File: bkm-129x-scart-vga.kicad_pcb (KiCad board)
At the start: 2 copper layers, 105 x 160 mm, 69 parts, among them J1 DB15_Female_HighDensity_Mount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, J2 SCART-F, J3 SJ1-353XNG, J4 UART, J5 Conn_02x32_Row_Letter_Last, J6 ICSP, Q1 DTC144EKA, Q2 MMBT3904, SW1 PBH4UEENAGX, SW2 PBH4UEENAGX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

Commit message: Add github link to PCB silkscreen.
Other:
- board text added: "(2020) Martin Hejnfelt (martin@hejnfelt.com) www.immerhax.com Mod github.com/proboterror/bkm-129x-scart-vga"
- board text removed: "(2020) Martin Hejnfelt (martin@hejnfelt.com) www.immerhax.com"
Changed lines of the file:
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@@
 		(layer "Edge.Cuts")
 	)
-	(gr_text "(2020) Martin Hejnfelt (martin@hejnfelt.com)\nwww.immerhax.com"
+	(gr_text "(2020) Martin Hejnfelt (martin@hejnfelt.com)\nwww.immerhax.com\n\nMod github.com/proboterror/bkm-129x-scart-vga"
 		(at 115.7478 50.3936 0)
 		(layer "B.SilkS")

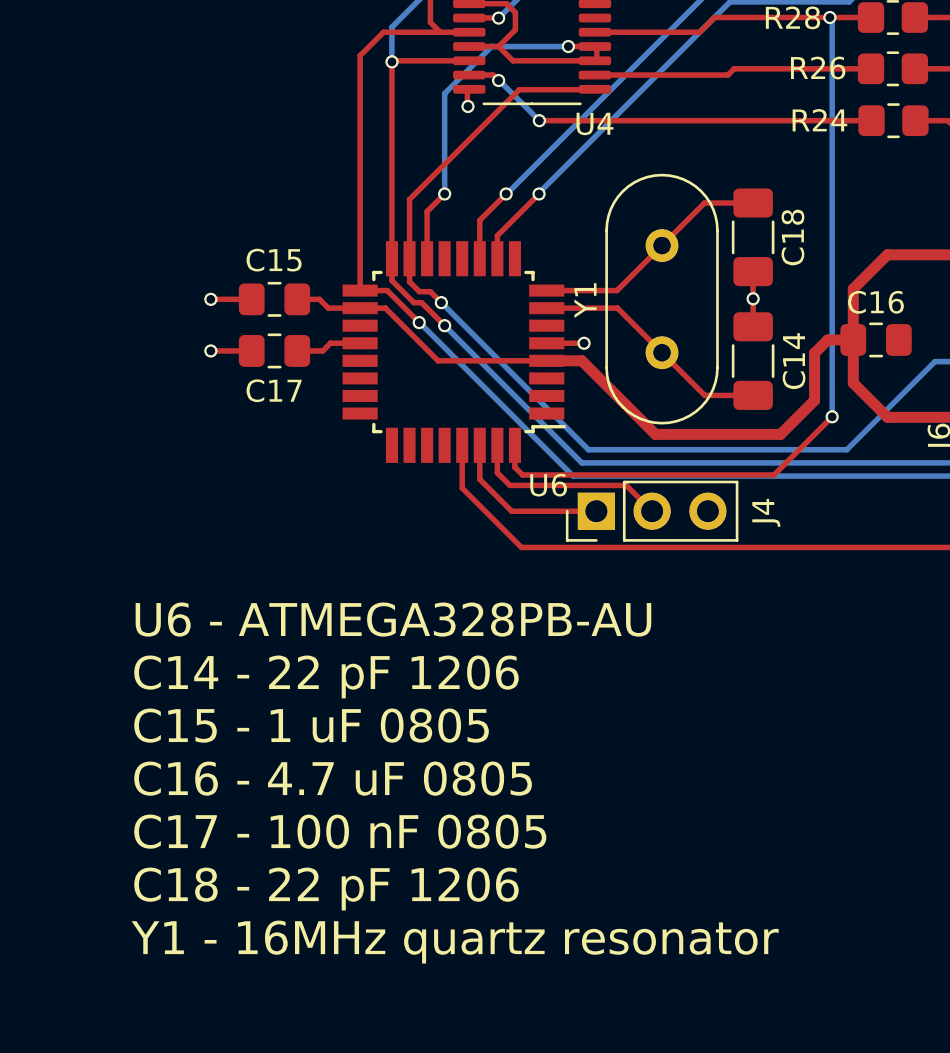
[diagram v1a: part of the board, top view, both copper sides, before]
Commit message: Change C14, C18 footprints from 1206 to 0805.
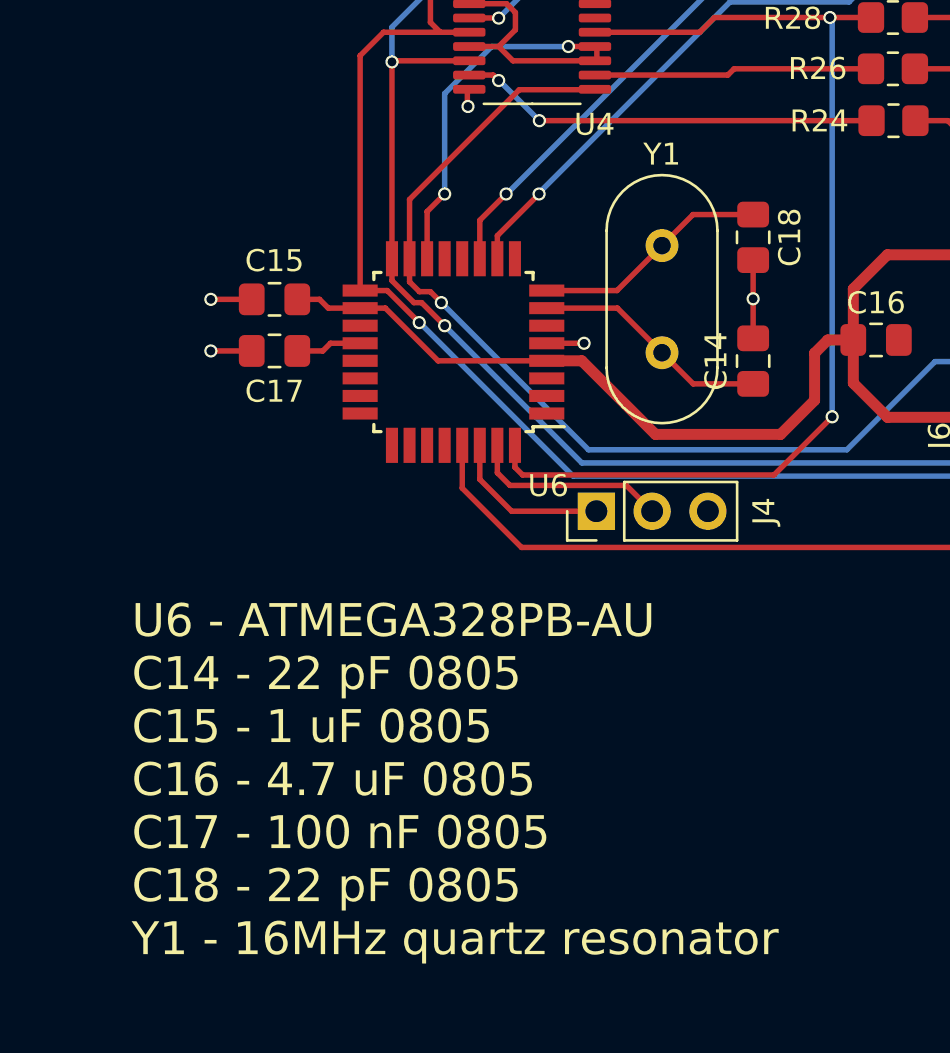
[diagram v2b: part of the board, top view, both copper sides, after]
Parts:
- C14, C18: footprint Capacitor_SMD:C_1206_3216Metric_Pad1.33x1.80mm_HandSolder -> Capacitor_SMD:C_0805_2012Metric_Pad1.18x1.45mm_HandSolder
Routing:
- net GNDA: track 20.5 -> 21.6 mm
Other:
- board text added: "U6 - ATMEGA328PB-AU C14 - 22 pF 0805 C15 - 1 uF 0805 C16 - 4.7 uF 0805 C17 - 100 nF 0805 C18 - 22 pF 0805 Y1 - 16MHz quartz resonator"
- board text removed: "U6 - ATMEGA328PB-AU C14 - 22 pF 1206 C15 - 1 uF 0805 C16 - 4.7 uF 0805 C17 - 100 nF 0805 C18 - 22 pF 1206 Y1 - 16MHz quartz resonator"
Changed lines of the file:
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@@
 		(tags "THT crystalHC-49/U")
 		(property "Reference" "Y1"
-			(at 2.44 3.45 90)
+			(at -4.15 0 180)
 			(layer "F.SilkS")
 			(effects
@@
 		)
 	)
-	(footprint "Capacitor_SMD:C_1206_3216Metric_Pad1.33x1.80mm_HandSolder"
+	(footprint "Capacitor_SMD:C_0805_2012Metric_Pad1.18x1.45mm_HandSolder"
 		(layer "F.Cu")
 		(at 110.6 134.675 -90)
-		(descr "Capacitor SMD 1206 (3216 Metric), square (rectangular) end terminal, IPC_7351 nominal with elongated pad for handsoldering. (Body size source: IPC-SM-782 page 76, https://www.pcb-3d.com/wordpress/wp-content/uploads/ipc-sm-782a_amendment_1_and_2.pdf), generated with kicad-footprint-generator")
+		(descr "Capacitor SMD 0805 (2012 Metric), square (rectangular) end terminal, IPC_7351 nominal with elongated pad for handsoldering. (Body size source: IPC-SM-782 page 76, https://www.pcb-3d.com/wordpress/wp-content/uploads/ipc-sm-782a_amendment_1_and_2.pdf, https://docs.google.com/spreadsheets/d/1BsfQQcO9C6DZCsRaXUlFlo91Tg2WpOkGARC1WS5S8t0/edit?usp=sharing), generated with kicad-footprint-generator")
 		(tags "capacitor handsolder")
 		(property "Reference" "C18"
-			(at 0 -1.85 90)
+			(at 0 -1.68 -90)
 			(layer "F.SilkS")
 			(effects
@@
 		)
 		(property "Value" "22pF"
-			(at 0.15 1.85 90)
+			(at 0 1.68 -90)
 			(layer "F.Fab")
 			(effects
@@
 			)
 		)
-		(property ki_fp_filters "C_*")
-		(sheetname "MCU")
-		(sheetfile "atmega328p.kicad_sch")
 		(attr smd)
 		(fp_line
-			(start -0.711252 0.91)
-			(end 0.711252 0.91)
+			(start -0.261252 0.735)
+			(end 0.261252 0.735)
 			(stroke
 				(width 0.12)
@@
 		)
 		(fp_line
-			(start -0.711252 -0.91)
-			(end 0.711252 -0.91)
+			(start -0.261252 -0.735)
+			(end 0.261252 -0.735)
 			(stroke
 				(width 0.12)
@@
 		)
 		(fp_line
-			(start -2.48 1.15)
-			(end -2.48 -1.15)
+			(start -1.88 0.98)
+			(end -1.88 -0.98)
 			(stroke
 				(width 0.05)
@@
 		)
 		(fp_line
-			(start 2.48 1.15)
-			(end -2.48 1.15)
+			(start 1.88 0.98)
+			(end -1.88 0.98)
 			(stroke
 				(width 0.05)
@@
 		)
 		(fp_line
-			(start -2.48 -1.15)
-			(end 2.48 -1.15)
+			(start -1.88 -0.98)
+			(end 1.88 -0.98)
 			(stroke
 				(width 0.05)
@@
 		)
 		(fp_line
-			(start 2.48 -1.15)
-			(end 2.48 1.15)
+			(start 1.88 -0.98)
+			(end 1.88 0.98)
 			(stroke
 				(width 0.05)
@@
 		)
 		(fp_line
-			(start -1.6 0.8)
-			(end -1.6 -0.8)
+			(start -1 0.625)
+			(end -1 -0.625)
 			(stroke
 				(width 0.1)
@@
 		)
 		(fp_line
-			(start 1.6 0.8)
-			(end -1.6 0.8)
+			(start 1 0.625)
+			(end -1 0.625)
 			(stroke
 				(width 0.1)
@@
 		)
 		(fp_line
-			(start -1.6 -0.8)
-			(end 1.6 -0.8)
+			(start -1 -0.625)
+			(end 1 -0.625)
 			(stroke
 				(width 0.1)
@@
 		)
 		(fp_line
-			(start 1.6 -0.8)
-			(end 1.6 0.8)
+			(start 1 -0.625)
+			(end 1 0.625)
 			(stroke
 				(width 0.1)
@@
 		)
 		(fp_text user "${REFERENCE}"
-			(at 0 0 90)
+			(at 0 0 -90)
 			(layer "F.Fab")
 			(effects
 				(font
-					(size 0.8 0.8)
-					(thickness 0.12)
+					(size 0.5 0.5)
+					(thickness 0.08)
 				)
 			)
 		)
 		(pad "1" smd roundrect
-			(at -1.5625 0 270)
-			(size 1.325 1.8)
+			(at -1.0375 0 270)
+			(size 1.175 1.45)
 			(layers "F.Cu" "F.Paste" "F.Mask")
-			(roundrect_rratio 0.188679)
+			(roundrect_rratio 0.212766)
 			(net 11 "Net-(U6-(XTAL2{slash}TOSC2)PB7)")
 			(pintype "passive")
 		)
 		(pad "2" smd roundrect
-			(at 1.5625 0 270)
-			(size 1.325 1.8)
+			(at 1.0375 0 270)
+			(size 1.175 1.45)
 			(layers "F.Cu" "F.Paste" "F.Mask")
-			(roundrect_rratio 0.188679)
+			(roundrect_rratio 0.212766)
 			(net 6 "GNDA")
 			(pintype "passive")
 		)
-		(model "${KICAD8_3DMODEL_DIR}/Capacitor_SMD.3dshapes/C_1206_3216Metric.wrl"
+		(model "${KICAD8_3DMODEL_DIR}/Capacitor_SMD.3dshapes/C_0805_2012Metric.wrl"
 			(offset
 				(xyz 0 0 0)
@@
 		)
 	)
-	(footprint "Capacitor_SMD:C_1206_3216Metric_Pad1.33x1.80mm_HandSolder"
+	(footprint "Capacitor_SMD:C_0805_2012Metric_Pad1.18x1.45mm_HandSolder"
 		(layer "F.Cu")
 		(at 110.6 140.3125 90)
-		(descr "Capacitor SMD 1206 (3216 Metric), square (rectangular) end terminal, IPC_7351 nominal with elongated pad for handsoldering. (Body size source: IPC-SM-782 page 76, https://www.pcb-3d.com/wordpress/wp-content/uploads/ipc-sm-782a_amendment_1_and_2.pdf), generated with kicad-footprint-generator")
+		(descr "Capacitor SMD 0805 (2012 Metric), square (rectangular) end terminal, IPC_7351 nominal with elongated pad for handsoldering. (Body size source: IPC-SM-782 page 76, https://www.pcb-3d.com/wordpress/wp-content/uploads/ipc-sm-782a_amendment_1_and_2.pdf, https://docs.google.com/spreadsheets/d/1BsfQQcO9C6DZCsRaXUlFlo91Tg2WpOkGARC1WS5S8t0/edit?usp=sharing), generated with kicad-footprint-generator")
 		(tags "capacitor handsolder")
 		(property "Reference" "C14"
-			(at 0 1.9 -90)
+			(at 0 -1.68 90)
 			(layer "F.SilkS")
 			(effects
@@
 		)
 		(property "Value" "22pF"
-			(at 0 -1.85 -90)
+			(at 0 1.68 90)
 			(layer "F.Fab")
 			(effects
@@
 			)
 		)
-		(property ki_fp_filters "C_*")
-		(sheetname "MCU")
-		(sheetfile "atmega328p.kicad_sch")
 		(attr smd)
 		(fp_line
-			(start -0.711252 -0.91)
-			(end 0.711252 -0.91)
+			(start -0.261252 -0.735)
+			(end 0.261252 -0.735)
 			(stroke
 				(width 0.12)
@@
 		)
 		(fp_line
-			(start -0.711252 0.91)
-			(end 0.711252 0.91)
+			(start -0.261252 0.735)
+			(end 0.261252 0.735)
 			(stroke
 				(width 0.12)
@@
 		)
 		(fp_line
-			(start 2.48 -1.15)
-			(end 2.48 1.15)
+			(start 1.88 -0.98)
+			(end 1.88 0.98)
 			(stroke
 				(width 0.05)
@@
 		)
 		(fp_line
-			(start -2.48 -1.15)
-			(end 2.48 -1.15)
+			(start -1.88 -0.98)
+			(end 1.88 -0.98)
 			(stroke
 				(width 0.05)
@@
 		)
 		(fp_line
-			(start 2.48 1.15)
-			(end -2.48 1.15)
+			(start 1.88 0.98)
+			(end -1.88 0.98)
 			(stroke
 				(width 0.05)
@@
 		)
 		(fp_line
-			(start -2.48 1.15)
-			(end -2.48 -1.15)
+			(start -1.88 0.98)
+			(end -1.88 -0.98)
 			(stroke
 				(width 0.05)
@@
 		)
 		(fp_line
-			(start 1.6 -0.8)
-			(end 1.6 0.8)
+			(start 1 -0.625)
+			(end 1 0.625)
 			(stroke
 				(width 0.1)
@@
 		)
 		(fp_line
-			(start -1.6 -0.8)
-			(end 1.6 -0.8)
+			(start -1 -0.625)
+			(end 1 -0.625)
 			(stroke
 				(width 0.1)
@@
 		)
 		(fp_line
-			(start 1.6 0.8)
-			(end -1.6 0.8)
+			(start 1 0.625)
+			(end -1 0.625)
 			(stroke
 				(width 0.1)
@@
 		)
 		(fp_line
-			(start -1.6 0.8)
-			(end -1.6 -0.8)
+			(start -1 0.625)
+			(end -1 -0.625)
 			(stroke
 				(width 0.1)
@@
 		)
 		(fp_text user "${REFERENCE}"
-			(at 0 0 -90)
+			(at 0 0 90)
 			(layer "F.Fab")
 			(effects
 				(font
-					(size 0.8 0.8)
-					(thickness 0.12)
+					(size 0.5 0.5)
+					(thickness 0.08)
 				)
 			)
 		)
 		(pad "1" smd roundrect
-			(at -1.5625 0 90)
-			(size 1.325 1.8)
+			(at -1.0375 0 90)
+			(size 1.175 1.45)
 			(layers "F.Cu" "F.Paste" "F.Mask")
-			(roundrect_rratio 0.188679)
+			(roundrect_rratio 0.212766)
 			(net 9 "Net-(U6-(XTAL1{slash}TOSC1)PB6)")
 			(pintype "passive")
 		)
 		(pad "2" smd roundrect
-			(at 1.5625 0 90)
-			(size 1.325 1.8)
+			(at 1.0375 0 90)
+			(size 1.175 1.45)
 			(layers "F.Cu" "F.Paste" "F.Mask")
-			(roundrect_rratio 0.188679)
+			(roundrect_rratio 0.212766)
 			(net 6 "GNDA")
 			(pintype "passive")
 		)
-		(model "${KICAD8_3DMODEL_DIR}/Capacitor_SMD.3dshapes/C_1206_3216Metric.wrl"
+		(model "${KICAD8_3DMODEL_DIR}/Capacitor_SMD.3dshapes/C_0805_2012Metric.wrl"
 			(offset
 				(xyz 0 0 0)
@@
 		)
 	)
-	(gr_text "U6 - ATMEGA328PB-AU\nC14 - 22 pF 1206\nC15 - 1 uF 0805\nC16 - 4.7 uF 0805\nC17 - 100 nF 0805\nC18 - 22 pF 1206\nY1 - 16MHz quartz resonator\n"
+	(gr_text "U6 - ATMEGA328PB-AU\nC14 - 22 pF 0805\nC15 - 1 uF 0805\nC16 - 4.7 uF 0805\nC17 - 100 nF 0805\nC18 - 22 pF 0805\nY1 - 16MHz quartz resonator\n"
 		(at 82.296 159.385 0)
 		(layer "F.SilkS")
@@
 	)
 	(segment
-		(start 110.6 136.2375)
-		(end 110.6 137.475)
-		(width 0.25)
-		(layer "F.Cu")
-		(net 6)
-	)
-	(segment
 		(start 102.235 99.2505)
 		(end 102.2438 99.2593)
@@
 	)
 	(segment
+		(start 110.6 135.7125)
+		(end 110.6 137.475)
+		(width 0.25)
+		(layer "F.Cu")
+		(net 6)
+	)
+	(segment
 		(start 87.7625 137.5)
 		(end 85.9 137.5)
@@
 	)
 	(segment
-		(start 110.6 138.75)
+		(start 110.6 139.275)
 		(end 110.6 137.475)
 		(width 0.25)
@@
 	)
 	(segment
-		(start 108.395 141.875)
+		(start 107.87 141.35)
 		(end 106.45 139.93)
 		(width 0.25)
@@
 	)
 	(segment
-		(start 110.6 141.875)
-		(end 108.395 141.875)
+		(start 110.6 141.35)
+		(end 107.87 141.35)
 		(width 0.25)
 		(layer "F.Cu")
@@
 	)
 	(segment
-		(start 108.3875 133.1125)
-		(end 106.45 135.05)
-		(width 0.25)
-		(layer "F.Cu")
-		(net 11)
-	)
-	(segment
 		(start 104.4 137.1)
 		(end 101.2 137.1)
@@
 	)
 	(segment
-		(start 110.6 133.1125)
-		(end 108.3875 133.1125)
-		(width 0.25)
-		(layer "F.Cu")
+		(start 110.6 133.6375)
+		(end 107.8625 133.6375)
+		(width 0.25)
+		(layer "F.Cu")
+		(net 11)
+	)
+	(segment
+		(start 107.8625 133.6375)
+		(end 106.45 135.05)
+		(width 0.25)
+		(layer "F.Cu")

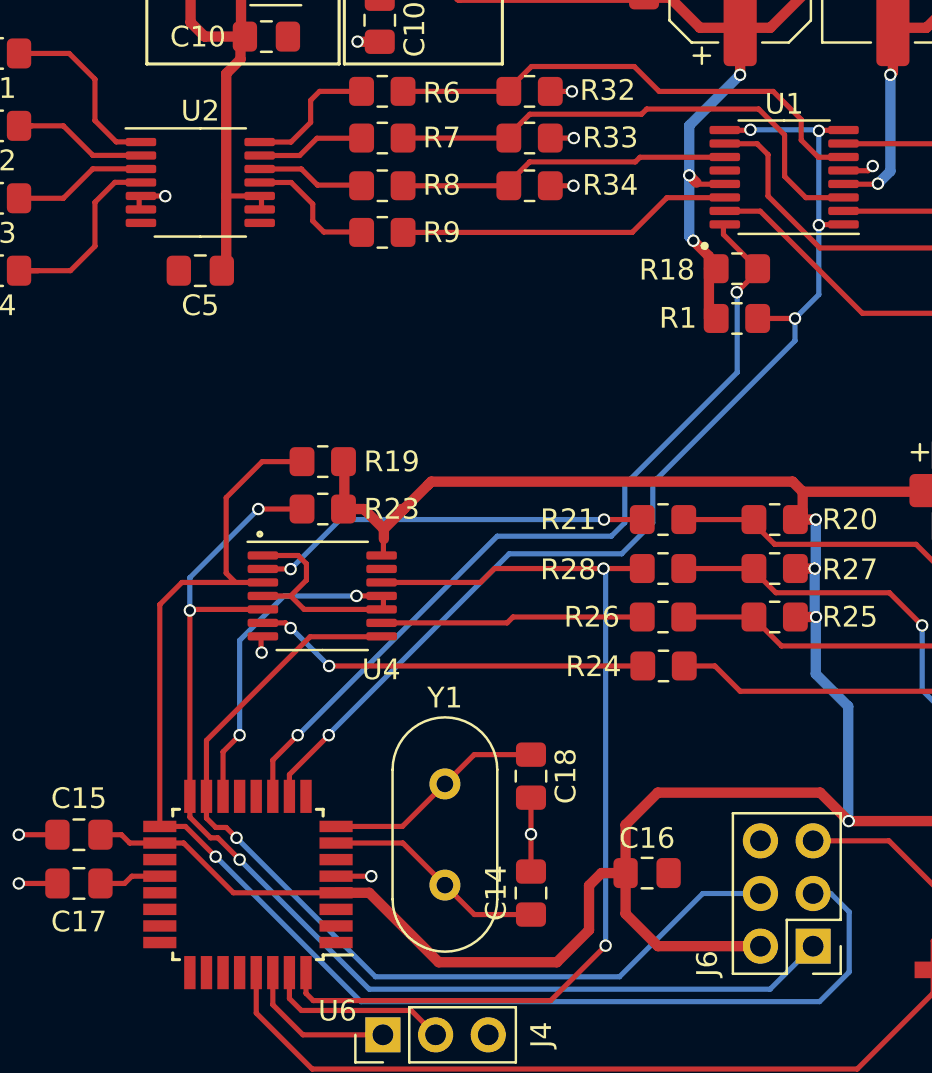
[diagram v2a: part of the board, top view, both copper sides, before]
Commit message: Change U4 footprint to TSSOP-14 (74LVC125AD.112).
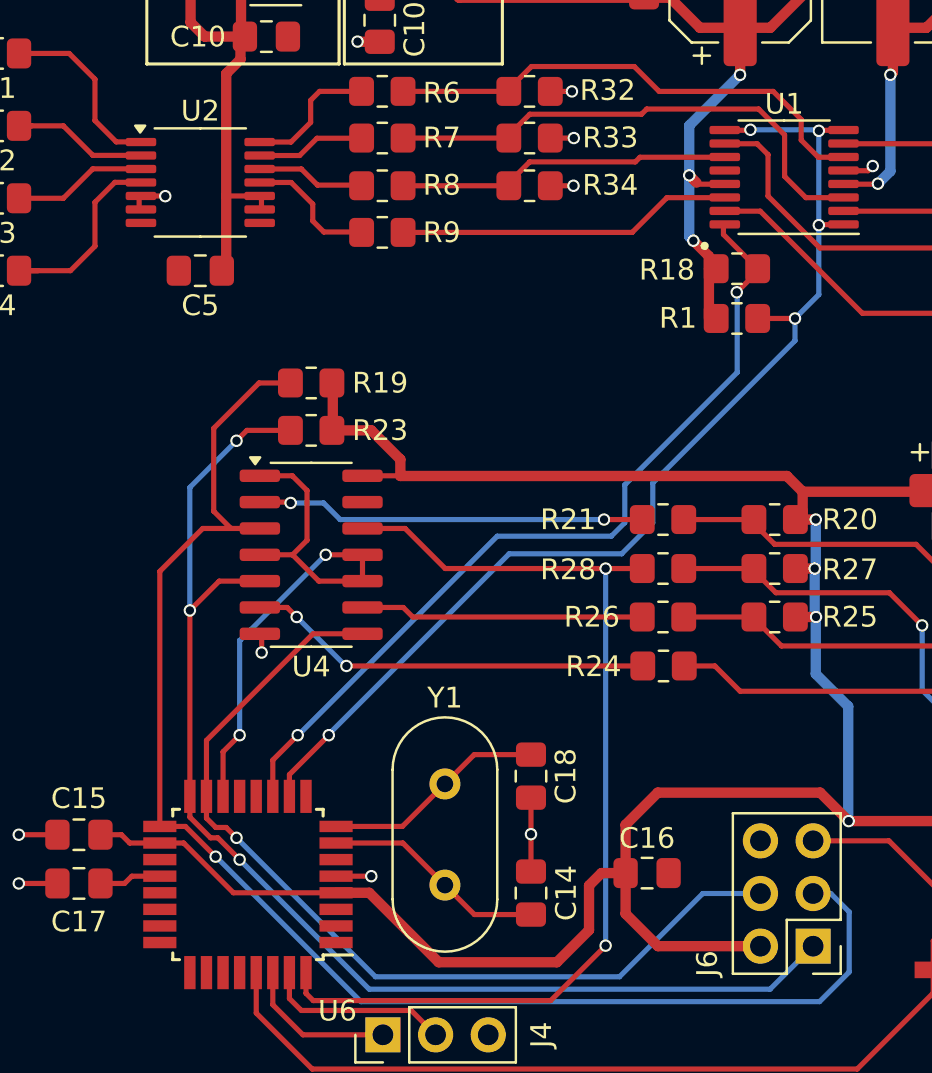
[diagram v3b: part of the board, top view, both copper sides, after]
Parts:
- U4: footprint Package_SO:TSSOP-14_4.4x5mm_P0.65mm -> Package_SO:SOIC-14_3.9x8.7mm_P1.27mm
- moved R19 3.83 mm to (100.0, 115.7)
- moved R23 3.83 mm to (100.0, 118.0)
- moved U4 2.05 mm to (100.0, 124.0)
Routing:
- net MCU_MISO: track 55.8 -> 60.2 mm
- net MCU_SCK: track 66.8 -> 70.1 mm
- net MCU_SLOT_ID: track 47.4 -> 49.4 mm
- net ~{MCU_SS}: track 26.7 -> 28.2 mm
- net Net-(U4C-D): track 12.3 -> 13.3 mm
- net +5VD: track 138.0 -> 139.0 mm
- net MCU_MOSI: track 45.9 -> 45.0 mm
- net Net-(U4A-D): track 19.0 -> 18.4 mm
